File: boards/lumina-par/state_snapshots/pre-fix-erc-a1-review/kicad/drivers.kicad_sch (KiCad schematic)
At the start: 68 parts, among them Q301 SSM3K2615R 60V 2A N-FET, Q321 SSM3K2615R 60V 2A N-FET, Q341 SSM3K2615R 60V 2A N-FET, Q361 SSM3K2615R 60V 2A N-FET, U301 TPS92515HVDGQR, U321 TPS92515HVDGQR, U341 TPS92515HVDGQR, U361 TPS92515HVDGQR

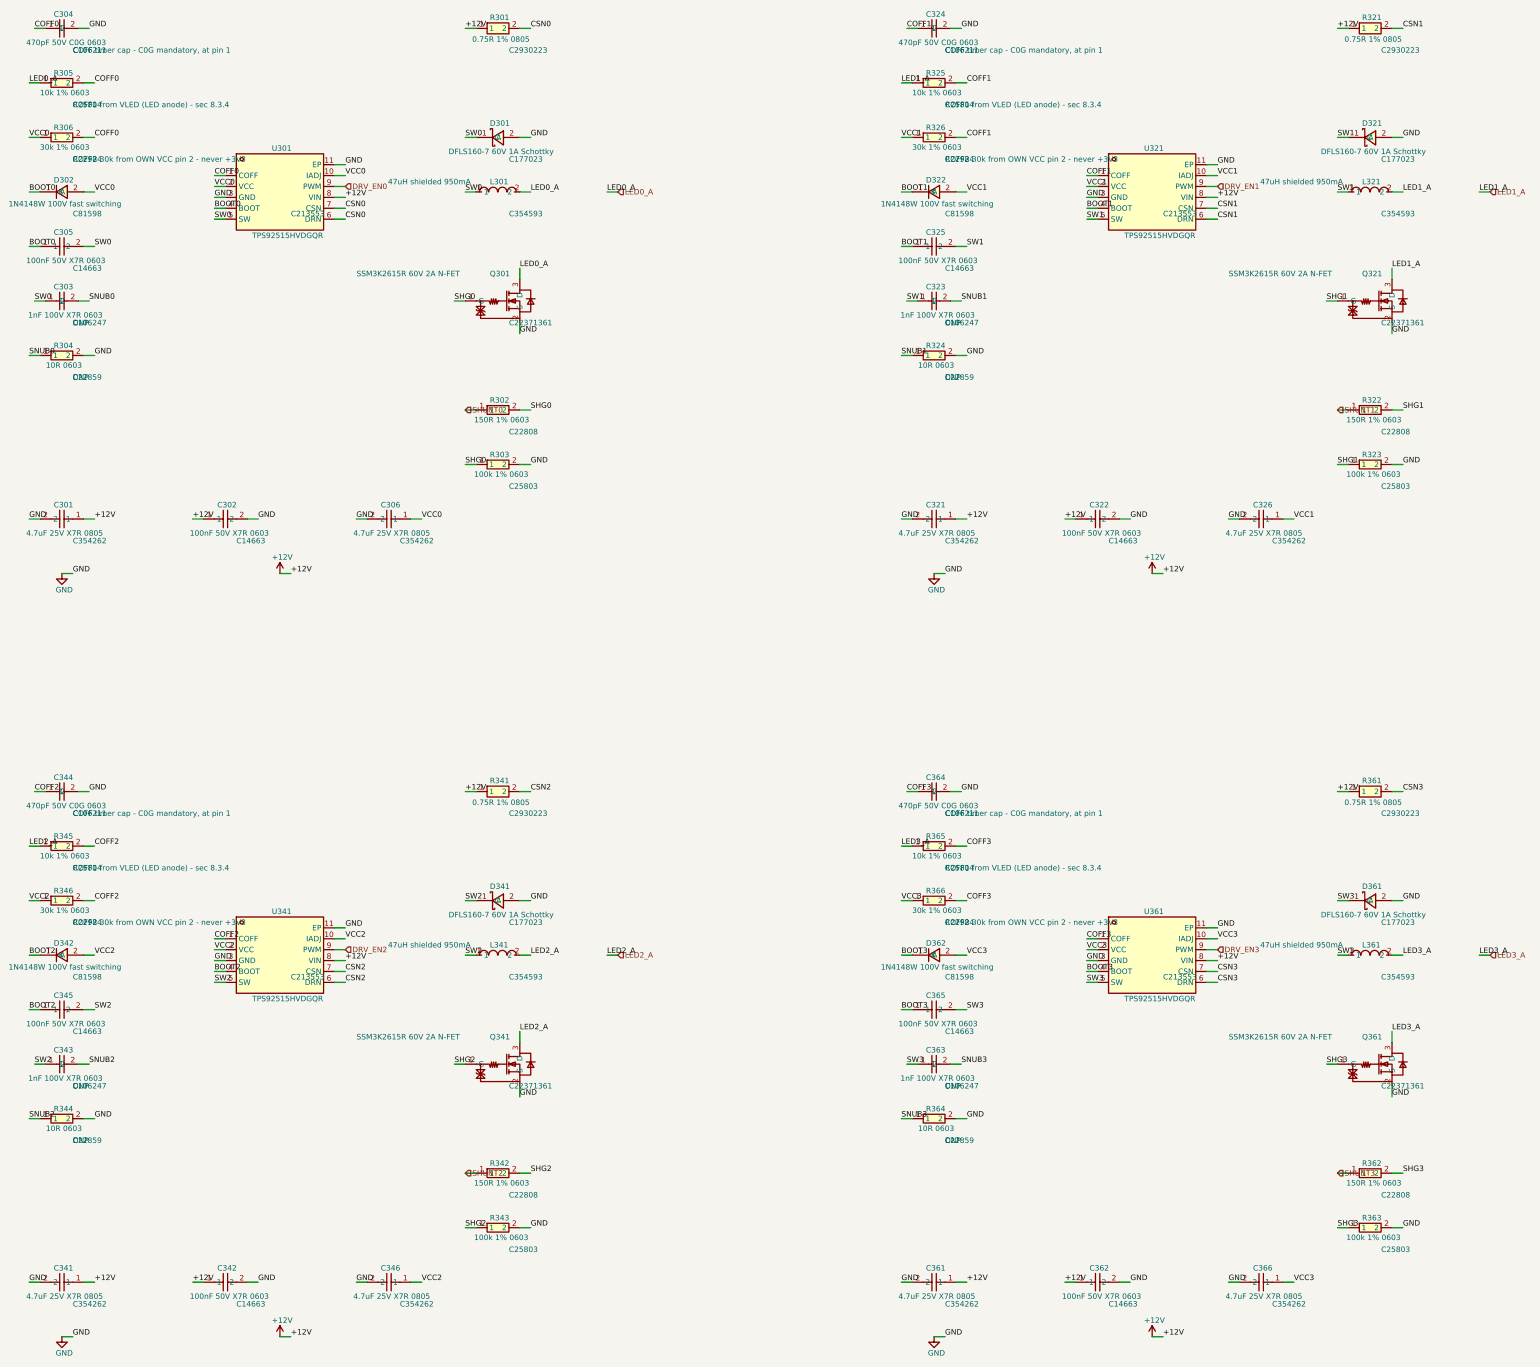
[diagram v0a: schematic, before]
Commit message: ai-ee lumina-par: erc pass after P4 review fixes (E-1 COFF values, E-2 NTC protection, E-3 DRV_EN pull-downs)
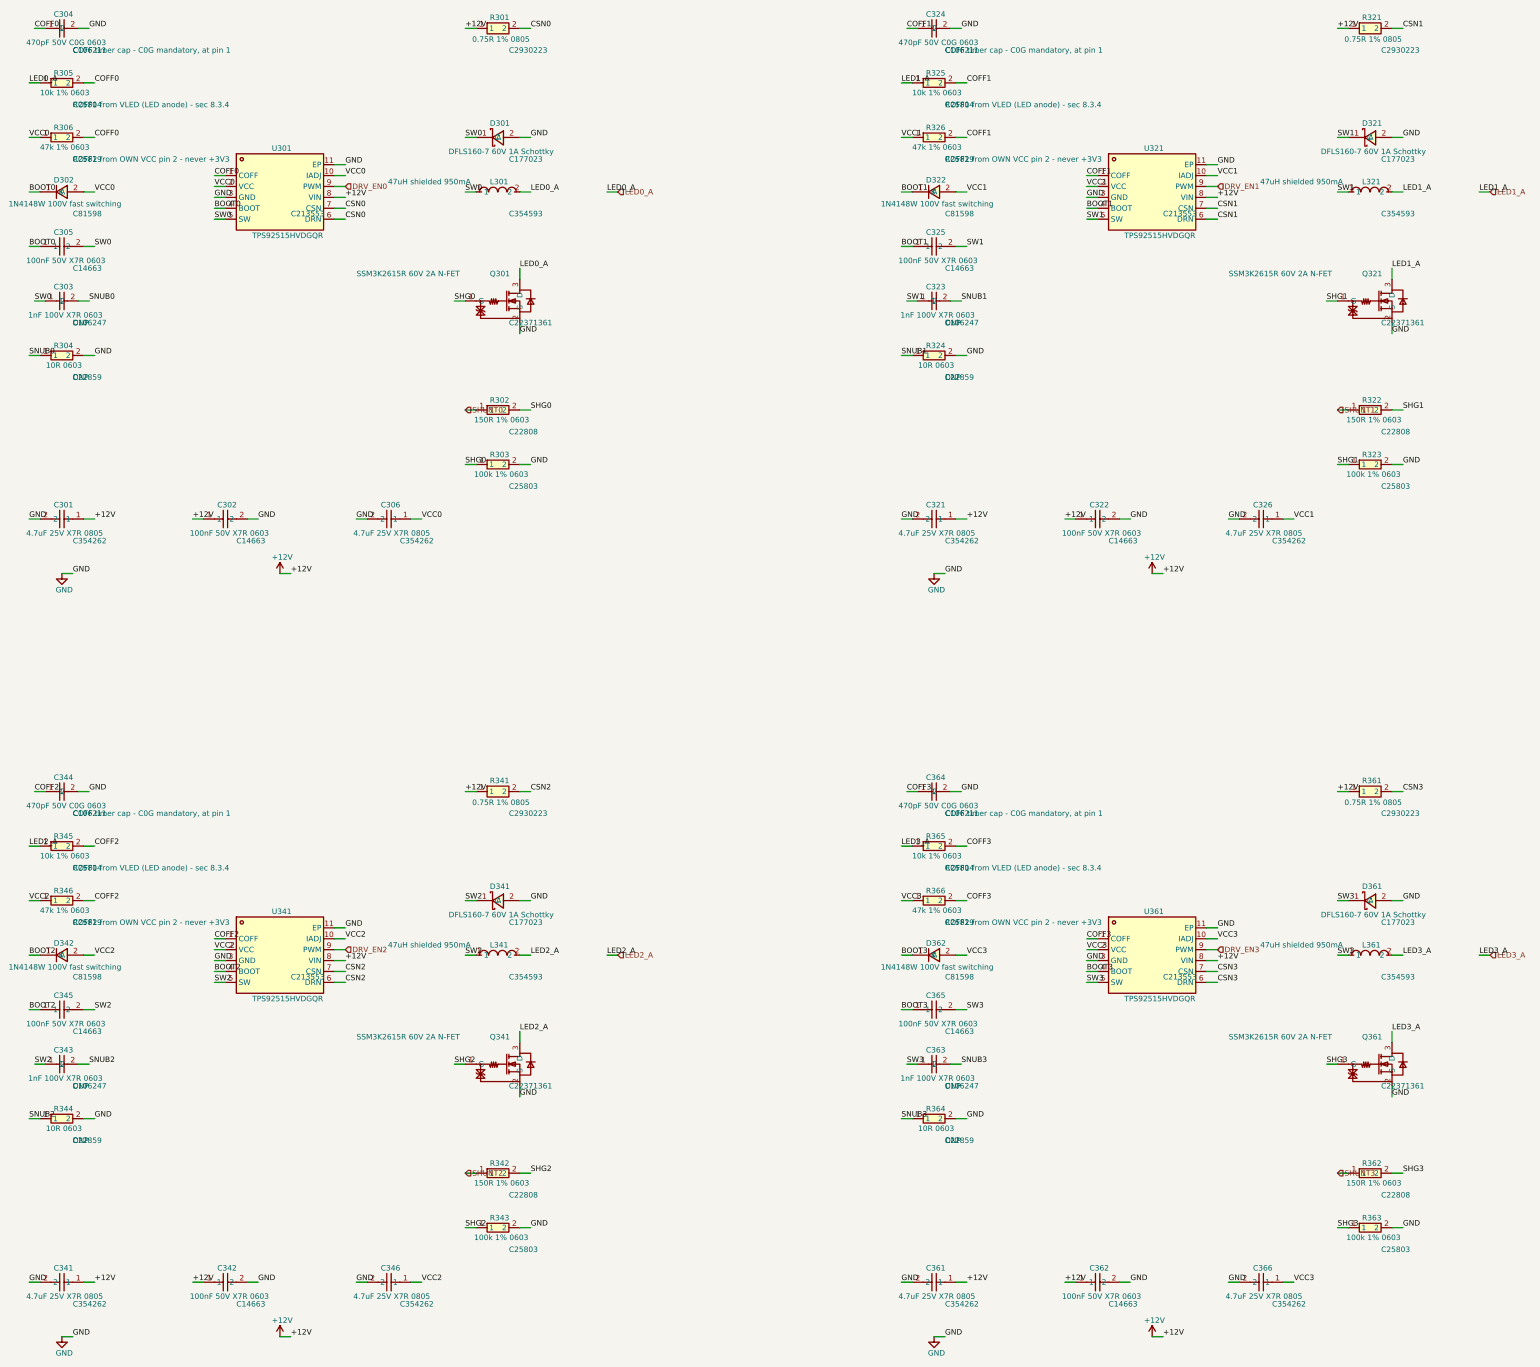
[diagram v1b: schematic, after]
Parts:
- removed R306, R326, R346, R366: 30k 1% 0603, aiee:R0603, symbol aiee:0603WAF2702T5E
- added R306, R326, R346, R366: 47k 1% 0603, aiee:R0603, symbol aiee:0603WAF4702T5E
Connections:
- net COFF0: now also R306.2
- net COFF1: now also R326.2
- net COFF2: now also R346.2
- net COFF3: now also R366.2
- net VCC0: now also R306.1
- net VCC1: now also R326.1
- net VCC2: now also R346.1
- net VCC3: now also R366.1
